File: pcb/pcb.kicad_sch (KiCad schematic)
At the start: 93 parts, among them J1 N!N, J10 Conn_01x12_Socket, J11 Conn_01x12_Socket, J12 Conn_01x02_Socket, J2 Conn_01x12_Socket, J3 Conn_01x12_Socket, J4 Conn_01x12_Socket, J5 Conn_01x12_Socket, J6 Display_nice-view, J7 Conn_01x02_Socket, J8 Conn_01x12_Socket, J9 Conn_01x12_Socket, SW1 Switch, SW10 Switch, SW11 Switch, SW12 Switch, SW13 Switch, SW14 Switch, SW15 Switch, SW16 Switch, SW17 Switch, SW18 Switch, SW19 Switch, SW2 Switch, SW20 Switch, SW21 Switch, SW22 Switch, SW23 Switch, SW24 Switch, SW25 Switch, SW26 Switch, SW27 Switch, SW28 Switch, SW29 Switch, SW3 Switch, SW30 Switch, SW31 Switch, SW32 Switch, SW33 Switch, SW34 Switch, SW35 Switch, SW36 Switch, SW37 SW_Push, SW38 RotaryEncoder_Switch, SW4 Switch, SW5 Switch, SW6 Switch, SW7 Switch, SW8 Switch, SW9 Switch

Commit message: second draft
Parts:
- added U1: RollerEncoder_EVQWGD001, zzkeeb:RotaryEncoder_EVQWGD001, symbol zzkeeb:RollerEncoder_EVQWGD001
- D1, D10, D11, D12, D13, D14, D15, D16, D17, D18, D2, D3, D4, D5, D6, D7, D8, D9: footprint zzkeeb:Diode_1N4148-SOD123-no-label-reversible -> zzkeeb:Diode_1N4148-SOD123
- D19, D20, D21, D22, D23, D24, D25, D26, D27, D28, D29, D30, D31, D32, D33, D34, D35, D36: footprint zzkeeb:Diode_1N4148-SOD123-no-label -> zzkeeb:Diode_1N4148-SOD123; now fitted
- H1, H2, H3, H4, H5, H6, H7: footprint zzkeeb:Hole_M2-TH -> zzkeeb:Hole_M2-solder-nut-2.5
- J12, SW19, SW20, SW21, SW22, SW23, SW24, SW25, SW26, SW27, SW28, SW29, SW30, SW31, SW32, SW33, SW34, SW35, SW36: now fitted
- SW1, SW10, SW11, SW12, SW13, SW14, SW15, SW16, SW17, SW18, SW2, SW3, SW4, SW5, SW6, SW7, SW8, SW9: footprint zzkeeb:Switch_KS-miny-reversible-hotswap-south -> zzkeeb:Switch_MXKS-miny-hotswap-south-ks3d
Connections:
- net col5-conn1 is gone; now on net col4-conn1: J10.2 (Pin_2), J8.2 (Pin_2)
- net col5-conn2 is gone; now on net col4-conn2: J11.2 (Pin_2), J9.2 (Pin_2)
- net col5-mcu is gone; now on net col4-mcu: J1.2 (008), J2.2 (Pin_2), J3.11 (Pin_11)
- net BAT-left: now also J4.1 (Pin_1); no longer J12.1 (Pin_1), J4.12 (Pin_12), J5.1 (Pin_1)
- net GND: now also J10.7 (Pin_7), J11.7 (Pin_7), J2.7 (Pin_7), J3.6 (Pin_6), J4.7 (Pin_7), J5.6 (Pin_6), J8.7 (Pin_7), J9.7 (Pin_7), U1.C, U1.S1; no longer J10.12 (Pin_12), J11.12 (Pin_12), J2.12 (Pin_12), J3.1 (Pin_1), J4.1 (Pin_1), J5.12 (Pin_12), J8.12 (Pin_12), J9.12 (Pin_12)
- net OFF: now also J1.31 (101), U1.S2; no longer J1.20 (031)
- net col0-conn1: now also J10.6 (Pin_6), J8.6 (Pin_6); no longer J10.7 (Pin_7), J8.7 (Pin_7)
- net col0-conn2: now also J11.6 (Pin_6), J9.6 (Pin_6); no longer J11.7 (Pin_7), J9.7 (Pin_7)
- net col0-mcu: now also J2.6 (Pin_6), J3.7 (Pin_7); no longer J2.7 (Pin_7), J3.6 (Pin_6)
- net col1-conn1: now also J10.5 (Pin_5), J8.5 (Pin_5); no longer J10.6 (Pin_6), J8.6 (Pin_6)
- net col1-conn2: now also J11.5 (Pin_5), J9.5 (Pin_5); no longer J11.6 (Pin_6), J9.6 (Pin_6)
- net col1-mcu: now also J2.5 (Pin_5), J3.8 (Pin_8); no longer J2.6 (Pin_6), J3.7 (Pin_7)
- net col2-conn1: now also J10.4 (Pin_4), J8.4 (Pin_4); no longer J10.5 (Pin_5), J8.5 (Pin_5)
- net col2-conn2: now also J11.4 (Pin_4), J9.4 (Pin_4); no longer J11.5 (Pin_5), J9.5 (Pin_5)
- net col2-mcu: now also J2.4 (Pin_4), J3.9 (Pin_9); no longer J2.5 (Pin_5), J3.8 (Pin_8)
- net col3-conn1: now also J10.3 (Pin_3), J8.3 (Pin_3); no longer J10.4 (Pin_4), J8.4 (Pin_4)
- net col3-conn2: now also J11.3 (Pin_3), J9.3 (Pin_3); no longer J11.4 (Pin_4), J9.4 (Pin_4)
- net col3-mcu: now also J1.20 (031), J2.3 (Pin_3), J3.10 (Pin_10); no longer J1.8 (024), J2.4 (Pin_4), J3.9 (Pin_9)
- net col4-conn1: no longer J10.3 (Pin_3), J8.3 (Pin_3)
- net col4-conn2: no longer J11.3 (Pin_3), J9.3 (Pin_3)
- net col4-mcu: no longer J1.7 (022), J2.3 (Pin_3), J3.10 (Pin_10)
- net encA: now also J1.7 (022), U1.A; no longer J1.31 (101)
- net encB: now also J1.8 (024), U1.B; no longer J1.32 (102)
- net row0: now also J4.11 (Pin_11); no longer D19.1 (K), D20.1 (K), D21.1 (K), D22.1 (K), D23.1 (K), J4.2 (Pin_2), J5.11 (Pin_11)
- net row1: now also J4.10 (Pin_10); no longer D24.1 (K), D25.1 (K), D26.1 (K), D27.1 (K), D28.1 (K), J4.3 (Pin_3), J5.10 (Pin_10)
- net row2: now also J4.9 (Pin_9); no longer D29.1 (K), D30.1 (K), D31.1 (K), D32.1 (K), D33.1 (K), J4.4 (Pin_4), J5.9 (Pin_9)
- net row3: now also J4.8 (Pin_8); no longer D34.1 (K), D35.1 (K), D36.1 (K), J4.5 (Pin_5), J5.8 (Pin_8)
- net free1-mcu: now reaches J1.33 (107)
- net free1-mcu: now also J2.12 (Pin_12)
- net col0-left renamed col0
- net col0: no longer J5.7 (Pin_7), SW19.2, SW24.2, SW29.2
- removed net col1-left: J4.7 (Pin_7), J5.6 (Pin_6), SW12.2, SW2.2, SW20.2, SW25.2, SW30.2, SW7.2
- removed net col2-left: J4.8 (Pin_8), J5.5 (Pin_5), SW13.2, SW16.2, SW21.2, SW26.2, SW3.2, SW31.2, SW34.2, SW8.2
- removed net col3-left: J4.9 (Pin_9), J5.4 (Pin_4), SW14.2, SW17.2, SW22.2, SW27.2, SW32.2, SW35.2, SW4.2, SW9.2
- removed net col4-left: J4.10 (Pin_10), J5.3 (Pin_3), SW10.2, SW15.2, SW18.2, SW23.2, SW28.2, SW33.2, SW36.2, SW5.2
- net col5-left renamed row7
- net row7: now also D34.1 (K), D35.1 (K), D36.1 (K); no longer J4.11 (Pin_11)
- new net BAT-right: J12.1 (Pin_1), J5.12 (Pin_12)
- new net col1: J4.5 (Pin_5), SW12.2, SW2.2, SW7.2
- new net col2: J4.4 (Pin_4), SW13.2, SW16.2, SW3.2, SW8.2
- new net col3: J4.3 (Pin_3), SW14.2, SW17.2, SW4.2, SW9.2
- new net col4: J4.2 (Pin_2), SW10.2, SW15.2, SW18.2, SW5.2
- new net col5: J5.7 (Pin_7), SW19.2, SW24.2, SW29.2, SW34.2
- new net col6: J5.8 (Pin_8), SW20.2, SW25.2, SW30.2, SW35.2
- new net col7: J5.9 (Pin_9), SW21.2, SW26.2, SW31.2, SW36.2
- new net col8: J5.10 (Pin_10), SW22.2, SW27.2, SW32.2
- new net col9: J5.11 (Pin_11), SW23.2, SW28.2, SW33.2
- new net free-conn1: J10.12 (Pin_12), J8.12 (Pin_12)
- new net free-conn2: J11.12 (Pin_12), J9.12 (Pin_12)
- new net free2-mcu: J1.32 (102), J3.1 (Pin_1)
- new net row4: D19.1 (K), D20.1 (K), D21.1 (K), D22.1 (K), D23.1 (K), J5.5 (Pin_5)
- new net row5: D24.1 (K), D25.1 (K), D26.1 (K), D27.1 (K), D28.1 (K), J5.4 (Pin_4)
- new net row6: D29.1 (K), D30.1 (K), D31.1 (K), D32.1 (K), D33.1 (K), J5.3 (Pin_3)
- no-connect marks 1 -> 3
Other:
- moved on the sheet: SW38

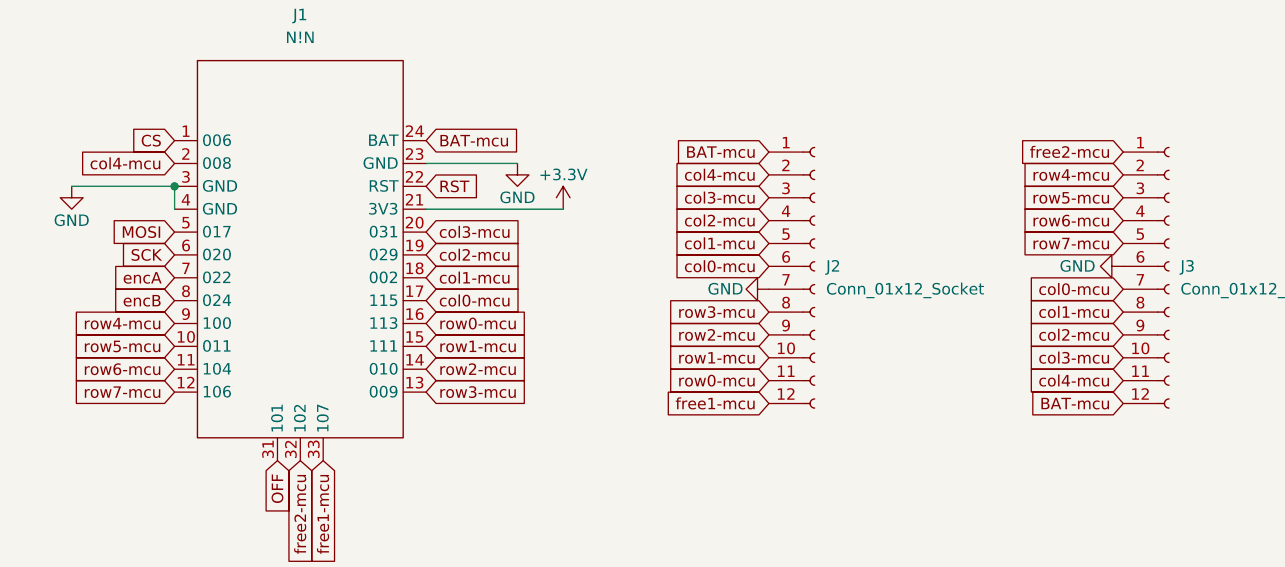
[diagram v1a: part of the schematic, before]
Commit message: update pin names
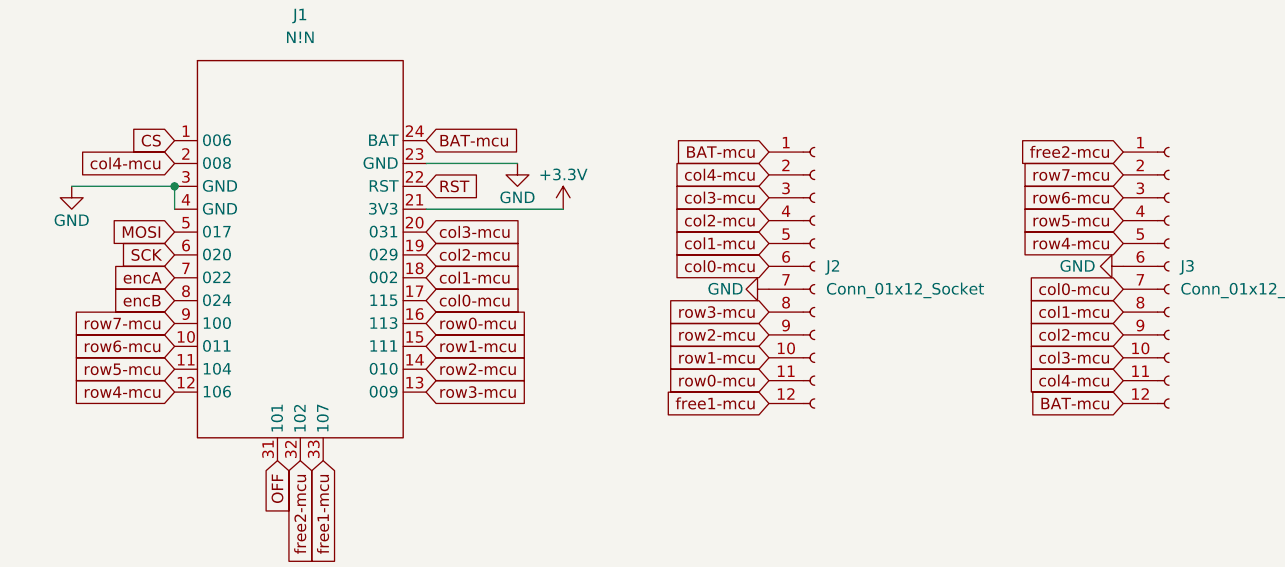
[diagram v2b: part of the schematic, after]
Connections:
- net row4-mcu: now also J1.12 (106), J3.5 (Pin_5); no longer J1.9 (100), J3.2 (Pin_2)
- net row5-mcu: now also J1.11 (104), J3.4 (Pin_4); no longer J1.10 (011), J3.3 (Pin_3)
- net row6-mcu: now also J1.10 (011), J3.3 (Pin_3); no longer J1.11 (104), J3.4 (Pin_4)
- net row7-mcu: now also J1.9 (100), J3.2 (Pin_2); no longer J1.12 (106), J3.5 (Pin_5)

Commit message: update case and main pcb
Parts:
- removed U1: RollerEncoder_EVQWGD001, zzkeeb:RotaryEncoder_EVQWGD001, symbol zzkeeb:RollerEncoder_EVQWGD001
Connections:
- no-connect marks 3 -> 2
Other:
- moved on the sheet: J6, SW37, SW38

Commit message: pcba version
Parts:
- D1, D10, D11, D12, D13, D14, D15, D16, D17, D18, D19, D2, D20, D21, D22, D23, D24, D25, D26, D27, D28, D29, D3, D30, D31, D32, D33, D34, D35, D36, D4, D5, D6, D7, D8, D9: value D -> C81598
- J2, J3, J4, J5: value Conn_01x12_Socket -> C479750
- J8, J9: value Conn_01x12_Socket -> C262499
- SW1, SW10, SW11, SW12, SW13, SW14, SW15, SW19, SW2, SW20, SW21, SW22, SW23, SW24, SW25, SW26, SW27, SW28, SW29, SW3, SW30, SW31, SW32, SW33, SW4, SW5, SW6, SW7, SW8, SW9: footprint zzkeeb:Switch_MXKS-miny-hotswap-south-ks3d -> zzkeeb:Switch_MXKSChoc-miny-hotswap-chocv2-3d
- SW16, SW17, SW18, SW34, SW35, SW36: footprint zzkeeb:Switch_MXKS-miny-hotswap-south-ks3d -> zzkeeb:Switch_KSChoc-miny-hotswap-chocv2-3d
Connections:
- net BAT-conn2: now also J9.12 (Pin_12); no longer J9.1 (Pin_1)
- net GND: now also J9.6 (Pin_6); no longer J9.7 (Pin_7)
- net col0-conn2: now also J9.7 (Pin_7); no longer J9.6 (Pin_6)
- net col1-conn2: now also J9.8 (Pin_8); no longer J9.5 (Pin_5)
- net col2-conn2: now also J9.9 (Pin_9); no longer J9.4 (Pin_4)
- net col3-conn2: now also J9.10 (Pin_10); no longer J9.3 (Pin_3)
- net col4-conn2: now also J9.11 (Pin_11); no longer J9.2 (Pin_2)
- net free-conn2: now also J9.1 (Pin_1); no longer J9.12 (Pin_12)
- net row0-conn2: now also J9.2 (Pin_2); no longer J9.11 (Pin_11)
- net row1-conn2: now also J9.3 (Pin_3); no longer J9.10 (Pin_10)
- net row2-conn2: now also J9.4 (Pin_4); no longer J9.9 (Pin_9)
- net row3-conn2: now also J9.5 (Pin_5); no longer J9.8 (Pin_8)

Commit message: small updates
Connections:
- net GND: now also SW37.1; no longer SW37.2
- net RST: now also SW37.2; no longer SW37.1
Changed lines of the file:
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@@
 		)
 	)
+	(global_label "RST"
+		(shape input)
+		(at 214.63 78.74 0)
+		(fields_autoplaced yes)
+		(effects
+			(font
+				(size 1.27 1.27)
+			)
+			(justify left)
+		)
+		(property "Intersheetrefs" "${INTERSHEET_REFS}"
+			(at 221.0623 78.74 0)
+			(effects
+				(font
+					(size 1.27 1.27)
+				)
+				(justify left)
+				(hide yes)
+			)
+		)
+	)
 	(global_label "col3"
 		(shape input)
@@
 		)
 	)
-	(global_label "RST"
-		(shape input)
-		(at 204.47 78.74 180)
-		(fields_autoplaced yes)
-		(effects
-			(font
-				(size 1.27 1.27)
-			)
-			(justify right)
-		)
-		(property "Intersheetrefs" "${INTERSHEET_REFS}"
-			(at 198.0377 78.74 0)
-			(effects
-				(font
-					(size 1.27 1.27)
-				)
-				(justify right)
-				(hide yes)
-			)
-		)
-	)
 	(global_label "free1-mcu"
 		(shape input)
@@
 	)
 	(symbol
-		(lib_id "power:GND")
-		(at 214.63 78.74 0)
-		(unit 1)
-		(exclude_from_sim no)
-		(in_bom yes)
-		(on_board yes)
-		(dnp no)
-		(property "Reference" "#PWR06"
-			(at 214.63 85.09 0)
-			(effects
-				(font
-					(size 1.27 1.27)
-				)
-				(hide yes)
-			)
-		)
-		(property "Value" "GND"
-			(at 214.63 82.55 0)
-			(effects
-				(font
-					(size 1.27 1.27)
-				)
-			)
-		)
-		(property "Footprint" ""
-			(at 214.63 78.74 0)
-			(effects
-				(font
-					(size 1.27 1.27)
-				)
-				(hide yes)
-			)
-		)
-		(property "Datasheet" ""
-			(at 214.63 78.74 0)
-			(effects
-				(font
-					(size 1.27 1.27)
-				)
-				(hide yes)
-			)
-		)
-		(property "Description" ""
-			(at 214.63 78.74 0)
-			(effects
-				(font
-					(size 1.27 1.27)
-				)
-				(hide yes)
-			)
-		)
-		(pin "1"
-		)
-		(instances
-			(project "pcb"
-				(path "/2f68eba7-4e8a-4af0-a221-669d7c557d47"
-					(reference "#PWR06")
-					(unit 1)
-				)
-			)
-		)
-	)
-	(symbol
 		(lib_id "Connector:Conn_01x12_Socket")
 		(at 292.1 45.72 0)
@@
 					(unit 1)
 				)
+			)
+		)
+	)
+	(symbol
+		(lib_id "power:GND")
+		(at 204.47 78.74 0)
+		(unit 1)
+		(exclude_from_sim no)
+		(in_bom yes)
+		(on_board yes)
+		(dnp no)
+		(property "Reference" "#PWR06"
+			(at 204.47 85.09 0)
+			(effects
+				(font
+					(size 1.27 1.27)
+				)
+				(hide yes)
+			)
+		)
+		(property "Value" "GND"
+			(at 204.47 82.55 0)
+			(effects
+				(font
+					(size 1.27 1.27)
+				)
+			)
+		)
+		(property "Footprint" ""
+			(at 204.47 78.74 0)
+			(effects
+				(font
+					(size 1.27 1.27)
+				)
+				(hide yes)
+			)
+		)
+		(property "Datasheet" ""
+			(at 204.47 78.74 0)
+			(effects
+				(font
+					(size 1.27 1.27)
+				)
+				(hide yes)
+			)
+		)
+		(property "Description" ""
+			(at 204.47 78.74 0)
+			(effects
+				(font
+					(size 1.27 1.27)
+				)
+				(hide yes)
+			)
+		)
+		(pin "1"
+		)
+		(instances
+			(project "pcb"
+				(path "/2f68eba7-4e8a-4af0-a221-669d7c557d47"
+					(reference "#PWR06")
+					(unit 1)
+				)
